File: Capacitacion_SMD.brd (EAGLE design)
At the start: 100 x 80 mm, 37 parts, among them IC1 LDO3V3

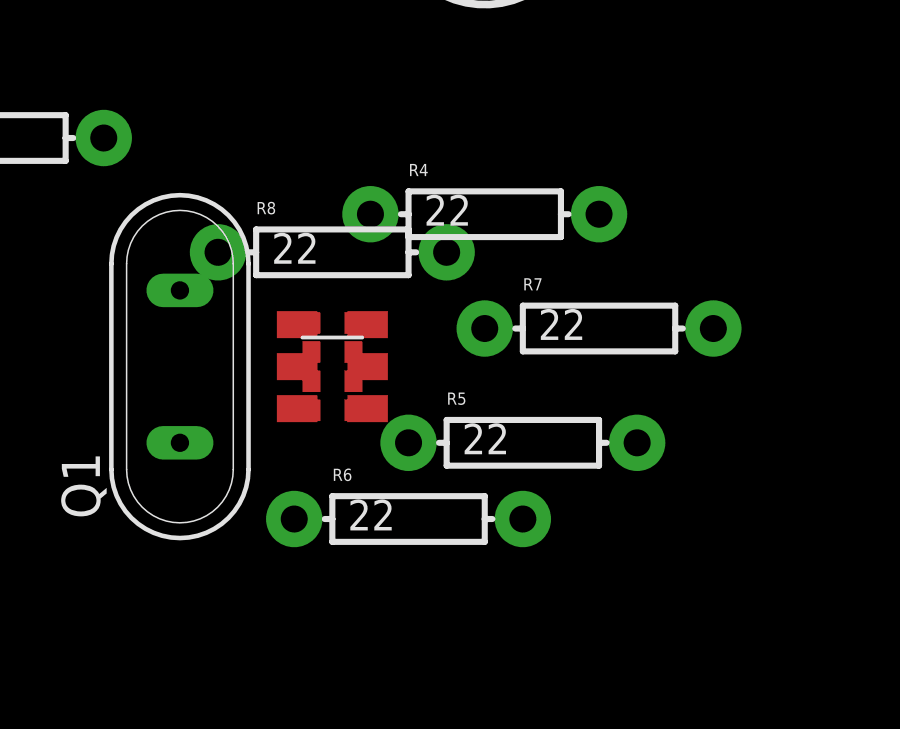
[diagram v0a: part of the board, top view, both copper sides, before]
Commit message: Values corrected for R7 & R8
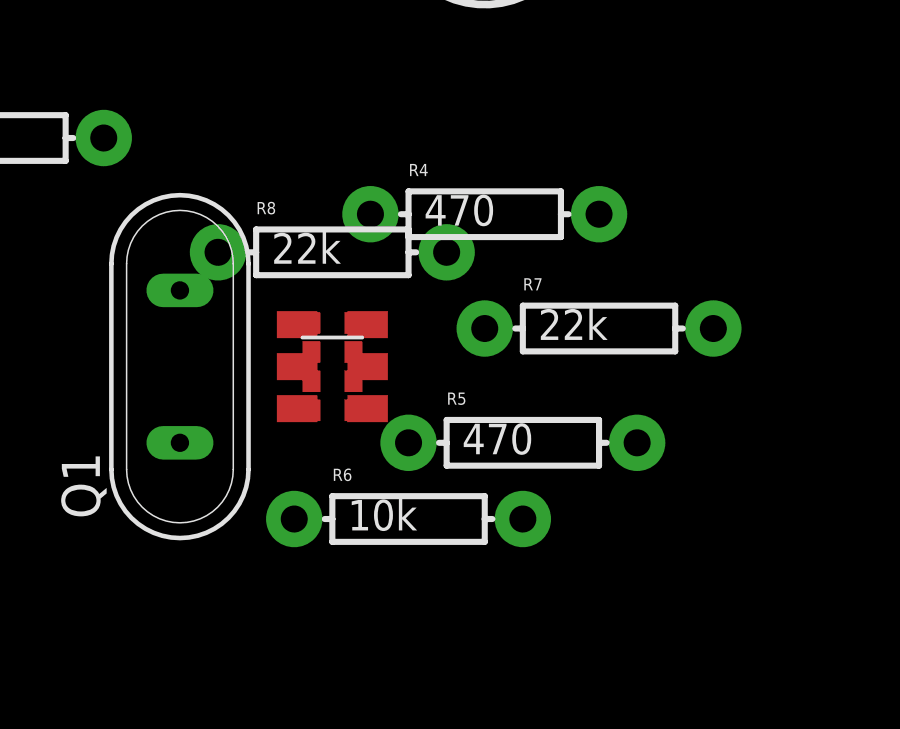
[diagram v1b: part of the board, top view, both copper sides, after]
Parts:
- R4, R5: value 22 -> 470
- R6: value 22 -> 10k
- R7, R8: value 22 -> 22k
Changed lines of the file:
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@@
 <element name="LED1" library="SparkFun-LED" package="LED5MM" value="" x="54.61" y="27.94"/>
 <element name="LED2" library="SparkFun-LED" package="LED5MM" value="" x="76.2" y="25.4"/>
-<element name="R4" library="SparkFun-Resistors" package="AXIAL-0.3" value="22" x="54.61" y="17.78"/>
-<element name="R5" library="SparkFun-Resistors" package="AXIAL-0.3" value="22" x="55.88" y="10.16"/>
+<element name="R4" library="SparkFun-Resistors" package="AXIAL-0.3" value="470" x="54.61" y="17.78"/>
+<element name="R5" library="SparkFun-Resistors" package="AXIAL-0.3" value="470" x="55.88" y="10.16"/>
 <element name="JP1" library="SparkFun-Connectors" package="1X12" value="M12PTH" x="2.54" y="2.54"/>
 <element name="JP2" library="SparkFun-Connectors" package="1X12" value="M12PTH" x="30.48" y="22.86" rot="R180"/>
 <element name="U$3" library="custom_components" package="RPI-1031" value="RPI-1031" x="49.53" y="12.7"/>
-<element name="R6" library="SparkFun-Resistors" package="AXIAL-0.3" value="22" x="52.07" y="7.62"/>
-<element name="R7" library="SparkFun-Resistors" package="AXIAL-0.3" value="22" x="58.42" y="13.97"/>
-<element name="R8" library="SparkFun-Resistors" package="AXIAL-0.3" value="22" x="49.53" y="16.51"/>
+<element name="R6" library="SparkFun-Resistors" package="AXIAL-0.3" value="10k" x="52.07" y="7.62"/>
+<element name="R7" library="SparkFun-Resistors" package="AXIAL-0.3" value="22k" x="58.42" y="13.97"/>
+<element name="R8" library="SparkFun-Resistors" package="AXIAL-0.3" value="22k" x="49.53" y="16.51"/>
 <element name="IC1" library="v-reg" package="78XXL" value="LDO3V3" x="17.78" y="44.45" rot="R90"/>
 <element name="C4" library="SparkFun-Capacitors" package="CAP-PTH-SMALL-KIT" value="22pF" x="25.4" y="43.18" rot="R90">

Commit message: Added indicator LEDs
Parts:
- added LED3, LED4, LED5, LED6: (no value), SparkFun-LED:LED5MM
- added R16, R17, R18, R19: 470, SparkFun-Resistors:AXIAL-0.3
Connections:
- removed net N$26: JP2.5, U$1.30
- removed net N$27: JP2.6, U$1.12
- removed net N$28: JP2.7, U$1.26
- removed net N$29: JP2.8, U$1.32
- new net LED1_SIG: JP2.5, R16.P$2, U$1.30
- new net LED2_SIG: JP2.6, R17.P$2, U$1.12
- new net LED3_SIG: JP2.7, R18.P$2, U$1.26
- new net LED4_SIG: JP2.8, R19.P$2, U$1.32
- new net N$21: LED4.A, R17.P$1
- new net N$22: LED5.A, R18.P$1
- new net N$23: LED6.A, R19.P$1
- new net N$9: LED3.A, R16.P$1
- net GND: now also LED3.K, LED4.K, LED5.K, LED6.K
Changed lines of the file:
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@@
 <attribute name="PROD_ID" value="CAP-08370" x="85.09" y="39.37" size="1.778" layer="27" rot="R90" display="off"/>
 </element>
+<element name="LED3" library="SparkFun-LED" package="LED5MM" value="" x="57.15" y="5.08" rot="R90"/>
+<element name="LED4" library="SparkFun-LED" package="LED5MM" value="" x="64.77" y="5.08" rot="R90"/>
+<element name="LED5" library="SparkFun-LED" package="LED5MM" value="" x="72.39" y="5.08" rot="R90"/>
+<element name="LED6" library="SparkFun-LED" package="LED5MM" value="" x="80.01" y="5.08" rot="R90"/>
+<element name="R16" library="SparkFun-Resistors" package="AXIAL-0.3" value="470" x="86.36" y="6.35" rot="R90"/>
+<element name="R17" library="SparkFun-Resistors" package="AXIAL-0.3" value="470" x="90.17" y="6.35" rot="R90"/>
+<element name="R18" library="SparkFun-Resistors" package="AXIAL-0.3" value="470" x="93.98" y="6.35" rot="R90"/>
+<element name="R19" library="SparkFun-Resistors" package="AXIAL-0.3" value="470" x="97.79" y="6.35" rot="R90"/>
 </elements>
 <signals>
@@
 <contactref element="C7" pad="2"/>
 <contactref element="C6" pad="2"/>
+<contactref element="LED6" pad="K"/>
+<contactref element="LED5" pad="K"/>
+<contactref element="LED4" pad="K"/>
+<contactref element="LED3" pad="K"/>
+<wire x1="81.28" y1="40.767" x2="85.09" y2="40.767" width="0" layer="19" extent="1-1"/>
+<wire x1="77.47" y1="25.4" x2="81.28" y2="40.767" width="0" layer="19" extent="1-1"/>
 <wire x1="55.88" y1="27.94" x2="77.47" y2="25.4" width="0" layer="19" extent="1-1"/>
 <wire x1="54.61" y1="13.97" x2="55.88" y2="27.94" width="0" layer="19" extent="1-1"/>
 <wire x1="50.705" y1="14.1" x2="54.61" y2="13.97" width="0" layer="19" extent="1-1"/>
-<wire x1="45.72" y1="16.51" x2="50.705" y2="14.1" width="0" layer="19" extent="1-1"/>
+<wire x1="48.83" y1="13.185" x2="50.705" y2="14.1" width="0" layer="19" extent="1-1"/>
+<wire x1="45.72" y1="16.51" x2="48.83" y2="13.185" width="0" layer="19" extent="1-1"/>
 <wire x1="36.13964375" y1="13.972790625" x2="45.72" y2="16.51" width="0" layer="19" extent="1-1"/>
 <wire x1="32.179846875" y1="7.467409375" x2="36.13964375" y2="13.972790625" width="0" layer="19" extent="1-1"/>
@@
 <wire x1="2.54" y1="22.86" x2="8.89" y2="11.45" width="0" layer="19" extent="1-1"/>
 <wire x1="41.783" y1="35.56" x2="36.957" y2="22.86" width="0" layer="19" extent="1-1"/>
-<wire x1="21.59" y1="44.45" x2="8.89" y2="11.45" width="0" layer="19" extent="1-1"/>
-<wire x1="25.4" y1="44.577" x2="21.59" y2="44.45" width="0" layer="19" extent="1-1"/>
-<wire x1="29.21" y1="44.577" x2="25.4" y2="44.577" width="0" layer="19" extent="1-1"/>
-<wire x1="48.83" y1="13.185" x2="29.21" y2="44.577" width="0" layer="19" extent="1-1"/>
-<wire x1="81.28" y1="40.767" x2="48.83" y2="13.185" width="0" layer="19" extent="1-1"/>
-<wire x1="85.09" y1="40.767" x2="81.28" y2="40.767" width="0" layer="19" extent="1-1"/>
+<wire x1="29.21" y1="44.577" x2="41.783" y2="35.56" width="0" layer="19" extent="1-1"/>
+<wire x1="25.4" y1="44.577" x2="29.21" y2="44.577" width="0" layer="19" extent="1-1"/>
+<wire x1="21.59" y1="44.45" x2="25.4" y2="44.577" width="0" layer="19" extent="1-1"/>
+<wire x1="57.15" y1="6.35" x2="13.2588" y2="6.6294" width="0" layer="19" extent="1-1"/>
+<wire x1="64.77" y1="6.35" x2="57.15" y2="6.35" width="0" layer="19" extent="1-1"/>
+<wire x1="72.39" y1="6.35" x2="64.77" y2="6.35" width="0" layer="19" extent="1-1"/>
+<wire x1="80.01" y1="6.35" x2="72.39" y2="6.35" width="0" layer="19" extent="1-1"/>
 </signal>
 <signal name="N$4">
@@
 <wire x1="32.74553125" y1="17.366903125" x2="22.86" y2="22.86" width="0" layer="19" extent="1-1"/>
 </signal>
-<signal name="N$26">
+<signal name="LED1_SIG">
 <contactref element="U$1" pad="30"/>
 <contactref element="JP2" pad="5"/>
-<wire x1="32.179846875" y1="17.9325875" x2="20.32" y2="22.86" width="0" layer="19" extent="1-1"/>
-</signal>
-<signal name="N$27">
+<contactref element="R16" pad="P$2"/>
+<wire x1="20.32" y1="22.86" x2="32.179846875" y2="17.9325875" width="0" layer="19" extent="1-1"/>
+<wire x1="86.36" y1="10.16" x2="32.179846875" y2="17.9325875" width="0" layer="19" extent="1-1"/>
+</signal>
+<signal name="LED2_SIG">
 <contactref element="U$1" pad="12"/>
 <contactref element="JP2" pad="6"/>
+<contactref element="R17" pad="P$2"/>
 <wire x1="30.482790625" y1="5.770353125" x2="17.78" y2="22.86" width="0" layer="19" extent="1-1"/>
-</signal>
-<signal name="N$28">
+<wire x1="90.17" y1="10.16" x2="30.482790625" y2="5.770353125" width="0" layer="19" extent="1-1"/>
+</signal>
+<signal name="LED3_SIG">
 <contactref element="U$1" pad="26"/>
 <contactref element="JP2" pad="7"/>
-<wire x1="34.4425875" y1="15.669846875" x2="15.24" y2="22.86" width="0" layer="19" extent="1-1"/>
-</signal>
-<signal name="N$29">
+<contactref element="R18" pad="P$2"/>
+<wire x1="15.24" y1="22.86" x2="34.4425875" y2="15.669846875" width="0" layer="19" extent="1-1"/>
+<wire x1="93.98" y1="10.16" x2="34.4425875" y2="15.669846875" width="0" layer="19" extent="1-1"/>
+</signal>
+<signal name="LED4_SIG">
 <contactref element="U$1" pad="32"/>
 <contactref element="JP2" pad="8"/>
-<wire x1="31.048475" y1="19.063959375" x2="12.7" y2="22.86" width="0" layer="19" extent="1-1"/>
+<contactref element="R19" pad="P$2"/>
+<wire x1="12.7" y1="22.86" x2="31.048475" y2="19.063959375" width="0" layer="19" extent="1-1"/>
+<wire x1="97.79" y1="10.16" x2="12.7" y2="22.86" width="0" layer="19" extent="1-1"/>
 </signal>
 <signal name="RXL_SIG">
@@
 <wire x1="48.83" y1="11.245" x2="81.28" y2="37.973" width="0" layer="19" extent="1-1"/>
 </signal>
+<signal name="N$9">
+<contactref element="R16" pad="P$1"/>
+<contactref element="LED3" pad="A"/>
+<wire x1="57.15" y1="3.81" x2="86.36" y2="2.54" width="0" layer="19" extent="1-1"/>
+</signal>
+<signal name="N$21">
+<contactref element="R17" pad="P$1"/>
+<contactref element="LED4" pad="A"/>
+<wire x1="64.77" y1="3.81" x2="90.17" y2="2.54" width="0" layer="19" extent="1-1"/>
+</signal>
+<signal name="N$22">
+<contactref element="R18" pad="P$1"/>
+<contactref element="LED5" pad="A"/>
+<wire x1="72.39" y1="3.81" x2="93.98" y2="2.54" width="0" layer="19" extent="1-1"/>
+</signal>
+<signal name="N$23">
+<contactref element="R19" pad="P$1"/>
+<contactref element="LED6" pad="A"/>
+<wire x1="80.01" y1="3.81" x2="97.79" y2="2.54" width="0" layer="19" extent="1-1"/>
+</signal>
 </signals>
